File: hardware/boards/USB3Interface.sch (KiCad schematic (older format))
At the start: 5 parts

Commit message: Updated part mfr and added the proper part numbers
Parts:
- removed J?: USB3_B, symbol Connector:USB3_B
- added J?: USB3_Micro_B_Amphenol, lethalbit:USB3_Micro_B_Amphenol, symbol lethalbit:USB3_Micro_B_Amphenol
- U?: value ECP5UM5G-381caBGA -> CYUSB3014; MFR (none) -> Lattice; MPN (none) -> LFE5UM5G-85F-8BG381I
- U? (x2): MFR (none) -> Cypress; MPN (none) -> CYUSB3014-BZXI
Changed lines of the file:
@@
 AR Path="/5F2CAFD2/5F2EB784" Ref="U?"  Part="3"
 F 0 "U?" H 9800 1548 50  0000 C CNN
-F 1 "ECP5UM5G-381caBGA" H 9800 1457 50  0000 C CNN
+F 1 "CYUSB3014" H 9800 1457 50  0000 C CNN
 F 2 "" H 8450 1350 50  0001 C CNN
 F 3 "" H 8450 1350 50  0001 C CNN
+F 4 "Lattice" H 9800 1200 50  0001 C CNN "MFR"
+F 5 "LFE5UM5G-85F-8BG381I" H 9800 1200 50  0001 C CNN "MPN"
 	3    9800 1200
 	1    0    0    -1
@@
 F 2 "" H 6400 4050 50  0001 C CNN
 F 3 "" H 6400 4050 50  0001 C CNN
+F 4 "Cypress" H 6400 3350 50  0001 C CNN "MFR"
+F 5 " CYUSB3014-BZXI" H 6400 3350 50  0001 C CNN "MPN"
 	2    6400 3350
 	1    0    0    -1
@@
 F 2 "" H 3050 2400 50  0001 C CNN
 F 3 "" H 3050 2400 50  0001 C CNN
+F 4 "Cypress" H 3050 1700 50  0001 C CNN "MFR"
+F 5 " CYUSB3014-BZXI" H 3050 1700 50  0001 C CNN "MPN"
 	3    3050 1700
 	1    0    0    -1
@@
 $EndComp
 $Comp
-L Connector:USB3_B J?
-U 1 1 5F338E59
-P 1200 1450
-F 0 "J?" H 1257 2167 50  0000 C CNN
-F 1 "USB3_B" H 1257 2076 50  0000 C CNN
-F 2 "" H 1350 1550 50  0001 C CNN
-F 3 "~" H 1350 1550 50  0001 C CNN
-	1    1200 1450
+L lethalbit:USB3_Micro_B_Amphenol J?
+U 1 1 5F8A43B9
+P 3050 2600
+F 0 "J?" H 3050 3125 50  0000 C CNN
+F 1 "USB3_Micro_B_Amphenol" H 3050 3034 50  0000 C CNN
+F 2 "lethalbit:USB3_Micro_B_Amphenol" H 3050 3050 50  0001 C CNN
+F 3 "https://www.amphenol-icc.com/media/wysiwyg/files/drawing/gsb343k33hr.pdf" H 3050 3050 50  0001 C CNN
+F 4 "Amphenol" H 3050 3050 50  0001 C CNN "MFR"
+F 5 "GSB343K33HR" H 3050 3050 50  0001 C CNN "MPN"
+	1    3050 2600
 	1    0    0    -1
 $EndComp

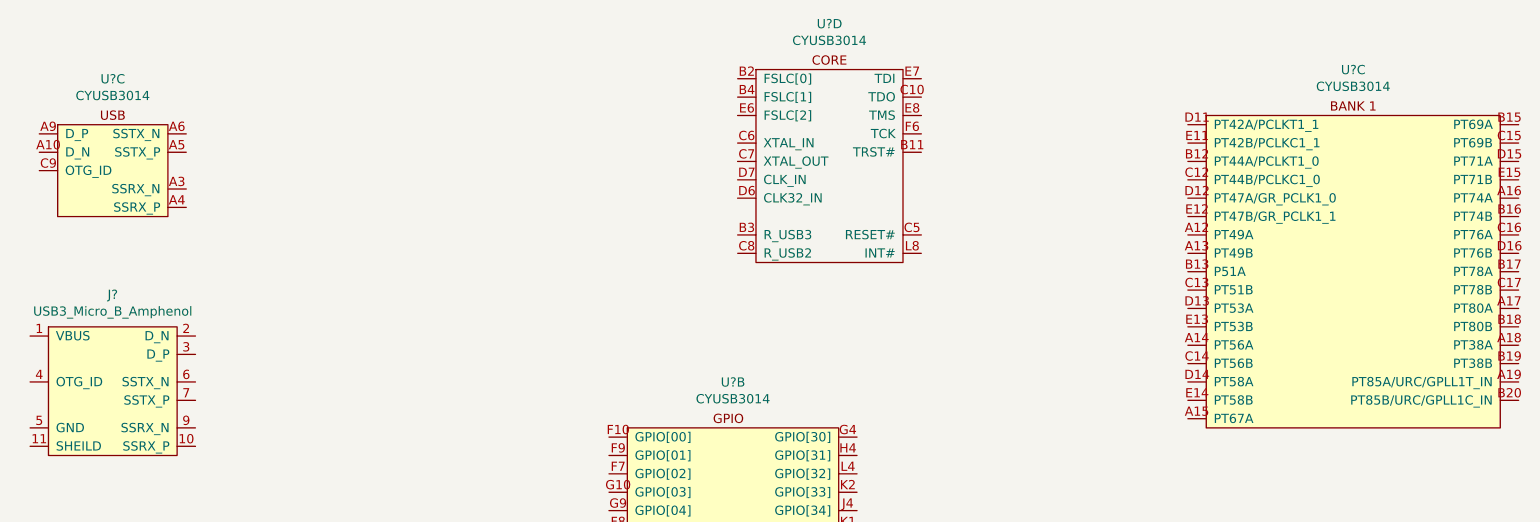
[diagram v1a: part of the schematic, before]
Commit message: Did some annotation and fixed the FPGA bank that was accidentally labled as the cypress part
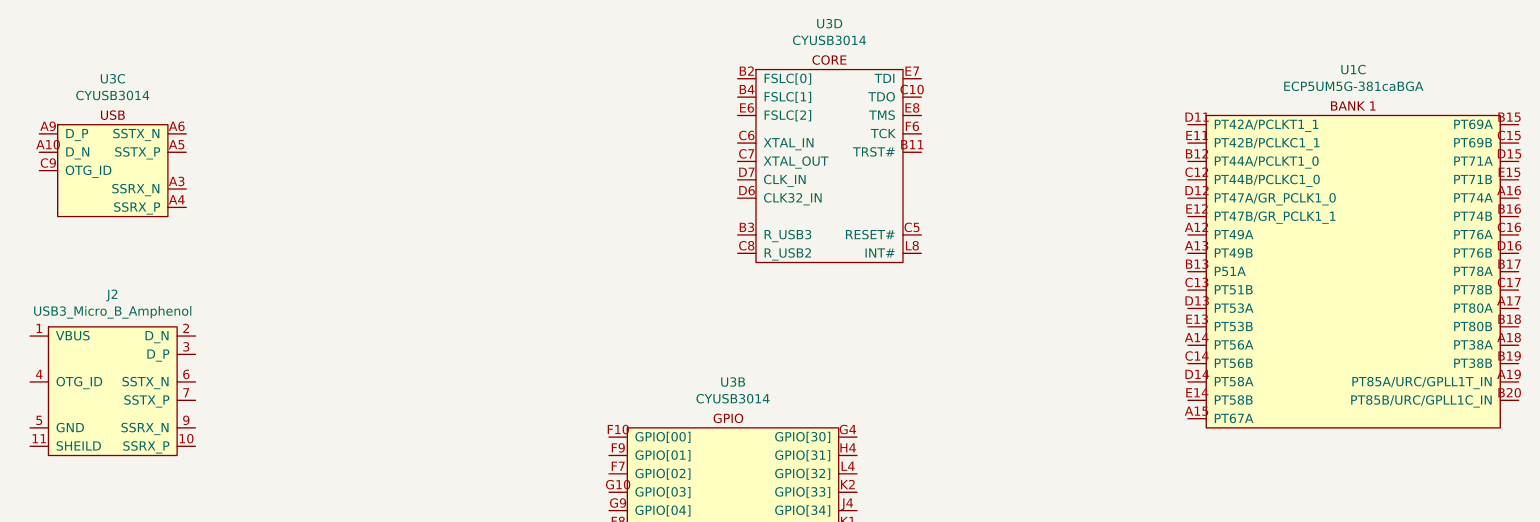
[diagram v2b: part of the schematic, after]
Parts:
- U1: renamed from U?; value CYUSB3014 -> ECP5UM5G-381caBGA; footprint (none) -> lethalbit:318caBGA
- U3: renamed from U?; footprint (none) -> lethalbit:BGA-121_11x11_10.0x10.0mm
- U3: renamed from U?; footprint (none) -> lethalbit:BGA-121_11x11_10.0x10.0mm; MFR (none) -> Cypress; MPN (none) -> https://www.cypress.com/file/140296/download
- gave numbers to parts that had none: 1
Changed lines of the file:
@@
 P 9800 1200
 AR Path="/5F2EB784" Ref="U?"  Part="3"
-AR Path="/5F2CAFD2/5F2EB784" Ref="U?"  Part="3"
-F 0 "U?" H 9800 1548 50  0000 C CNN
-F 1 "CYUSB3014" H 9800 1457 50  0000 C CNN
-F 2 "" H 8450 1350 50  0001 C CNN
+AR Path="/5F2CAFD2/5F2EB784" Ref="U1"  Part="3"
+F 0 "U1" H 9800 1548 50  0000 C CNN
+F 1 "ECP5UM5G-381caBGA" H 9800 1457 50  0000 C CNN
+F 2 "lethalbit:318caBGA" H 8450 1350 50  0001 C CNN
 F 3 "" H 8450 1350 50  0001 C CNN
 F 4 "Lattice" H 9800 1200 50  0001 C CNN "MFR"
@@
 $EndComp
 $Comp
-L lethalbit:CYUSB3014 U?
+L lethalbit:CYUSB3014 U3
 U 2 1 5F3318A9
 P 6400 3350
-F 0 "U?" H 6425 4148 50  0000 C CNN
+F 0 "U3" H 6425 4148 50  0000 C CNN
 F 1 "CYUSB3014" H 6425 4057 50  0000 C CNN
-F 2 "" H 6400 4050 50  0001 C CNN
-F 3 "" H 6400 4050 50  0001 C CNN
+F 2 "lethalbit:BGA-121_11x11_10.0x10.0mm" H 6400 4050 50  0001 C CNN
+F 3 "https://www.cypress.com/file/140296/download" H 6400 4050 50  0001 C CNN
 F 4 "Cypress" H 6400 3350 50  0001 C CNN "MFR"
 F 5 " CYUSB3014-BZXI" H 6400 3350 50  0001 C CNN "MPN"
@@
 $EndComp
 $Comp
-L lethalbit:CYUSB3014 U?
+L lethalbit:CYUSB3014 U3
 U 3 1 5F3336EC
 P 3050 1700
-F 0 "U?" H 3050 2498 50  0000 C CNN
+F 0 "U3" H 3050 2498 50  0000 C CNN
 F 1 "CYUSB3014" H 3050 2407 50  0000 C CNN
-F 2 "" H 3050 2400 50  0001 C CNN
-F 3 "" H 3050 2400 50  0001 C CNN
+F 2 "lethalbit:BGA-121_11x11_10.0x10.0mm" H 3050 2400 50  0001 C CNN
+F 3 "https://www.cypress.com/file/140296/download" H 3050 2400 50  0001 C CNN
 F 4 "Cypress" H 3050 1700 50  0001 C CNN "MFR"
 F 5 " CYUSB3014-BZXI" H 3050 1700 50  0001 C CNN "MPN"
@@
 $EndComp
 $Comp
-L lethalbit:CYUSB3014 U?
+L lethalbit:CYUSB3014 U3
 U 4 1 5F335021
 P 6950 1400
-F 0 "U?" H 6950 2198 50  0000 C CNN
+F 0 "U3" H 6950 2198 50  0000 C CNN
 F 1 "CYUSB3014" H 6950 2107 50  0000 C CNN
-F 2 "" H 6950 2100 50  0001 C CNN
-F 3 "" H 6950 2100 50  0001 C CNN
+F 2 "lethalbit:BGA-121_11x11_10.0x10.0mm" H 6950 2100 50  0001 C CNN
+F 3 "https://www.cypress.com/file/140296/download" H 6950 2100 50  0001 C CNN
+F 4 "Cypress" H 6950 1400 50  0001 C CNN "MFR"
+F 5 "https://www.cypress.com/file/140296/download" H 6950 1400 50  0001 C CNN "MPN"
 	4    6950 1400
 	1    0    0    -1
 $EndComp
 $Comp
-L lethalbit:USB3_Micro_B_Amphenol J?
+L lethalbit:USB3_Micro_B_Amphenol J2
 U 1 1 5F8A43B9
 P 3050 2600
-F 0 "J?" H 3050 3125 50  0000 C CNN
+F 0 "J2" H 3050 3125 50  0000 C CNN
 F 1 "USB3_Micro_B_Amphenol" H 3050 3034 50  0000 C CNN
 F 2 "lethalbit:USB3_Micro_B_Amphenol" H 3050 3050 50  0001 C CNN

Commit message: Some more mist schematic edits
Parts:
- J2: DIGIKEY_PN (none) -> GSB343K33HRCT-ND
- U1: DIGIKEY_PN (none) -> 220-2112-ND
- U3: DIGIKEY_PN (none) -> 428-3130-ND
- U3: DIGIKEY_PN (none) -> 428-3130-ND; MPN https://www.cypress.com/file/140296/download -> CYUSB3014-BZXI
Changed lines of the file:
@@
 F 4 "Lattice" H 9800 1200 50  0001 C CNN "MFR"
 F 5 "LFE5UM5G-85F-8BG381I" H 9800 1200 50  0001 C CNN "MPN"
+F 6 "220-2112-ND" H 9800 1200 50  0001 C CNN "DIGIKEY_PN"
 	3    9800 1200
 	1    0    0    -1
@@
 F 4 "Cypress" H 6400 3350 50  0001 C CNN "MFR"
 F 5 " CYUSB3014-BZXI" H 6400 3350 50  0001 C CNN "MPN"
+F 6 "428-3130-ND" H 6400 3350 50  0001 C CNN "DIGIKEY_PN"
 	2    6400 3350
 	1    0    0    -1
@@
 F 4 "Cypress" H 3050 1700 50  0001 C CNN "MFR"
 F 5 " CYUSB3014-BZXI" H 3050 1700 50  0001 C CNN "MPN"
+F 6 "428-3130-ND" H 3050 1700 50  0001 C CNN "DIGIKEY_PN"
 	3    3050 1700
 	1    0    0    -1
@@
 F 3 "https://www.cypress.com/file/140296/download" H 6950 2100 50  0001 C CNN
 F 4 "Cypress" H 6950 1400 50  0001 C CNN "MFR"
-F 5 "https://www.cypress.com/file/140296/download" H 6950 1400 50  0001 C CNN "MPN"
+F 5 " CYUSB3014-BZXI" H 6950 1400 50  0001 C CNN "MPN"
+F 6 "428-3130-ND" H 6950 1400 50  0001 C CNN "DIGIKEY_PN"
 	4    6950 1400
 	1    0    0    -1
@@
 F 4 "Amphenol" H 3050 3050 50  0001 C CNN "MFR"
 F 5 "GSB343K33HR" H 3050 3050 50  0001 C CNN "MPN"
+F 6 "GSB343K33HRCT-ND" H 3050 2600 50  0001 C CNN "DIGIKEY_PN"
 	1    3050 2600
 	1    0    0    -1

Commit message: Lots of small updates, getting values specified for parts, switched the BJT to NFETs
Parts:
- added C39: 0.1uF, Capacitor_SMD:C_0603_1608Metric, symbol Device:C_Small
- added R35: 1M, Resistor_SMD:R_0603_1608Metric, symbol Device:R_Small
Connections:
- net at U3.A10 (D_N): now also J2.2 (D_N)
- net at U3.A3 (SSRX_N): now also J2.9 (SSRX_N)
- net at U3.A4 (SSRX_P): now also J2.10 (SSRX_P)
- net at U3.A5 (SSTX_P): now also J2.7 (SSTX_P)
- net at U3.A6 (SSTX_N): now also J2.6 (SSTX_N)
- net at U3.A9 (D_P): now also J2.3 (D_P)
- net at J2.11 (SHEILD): now also C39.2, R35.1
- net GND: now reaches J2.5 (GND), J2.8 (GND)
- net GND: now also C39.1, R35.2
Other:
- moved on the sheet: J2, U1C, U3B, U3D
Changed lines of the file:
@@
 $Descr A4 11693 8268
 encoding utf-8
-Sheet 10 11
+Sheet 7 10
 Title ""
 Date ""
@@
 L lethalbit:ECP5UM5G-381caBGA U?
 U 3 1 5F2EB784
-P 9800 1200
+P 7950 3750
 AR Path="/5F2EB784" Ref="U?"  Part="3"
 AR Path="/5F2CAFD2/5F2EB784" Ref="U1"  Part="3"
-F 0 "U1" H 9800 1548 50  0000 C CNN
-F 1 "ECP5UM5G-381caBGA" H 9800 1457 50  0000 C CNN
-F 2 "lethalbit:318caBGA" H 8450 1350 50  0001 C CNN
-F 3 "" H 8450 1350 50  0001 C CNN
-F 4 "Lattice" H 9800 1200 50  0001 C CNN "MFR"
-F 5 "LFE5UM5G-85F-8BG381I" H 9800 1200 50  0001 C CNN "MPN"
-F 6 "220-2112-ND" H 9800 1200 50  0001 C CNN "DIGIKEY_PN"
-	3    9800 1200
+F 0 "U1" H 7950 4098 50  0000 C CNN
+F 1 "ECP5UM5G-381caBGA" H 7950 4007 50  0000 C CNN
+F 2 "lethalbit:318caBGA" H 6600 3900 50  0001 C CNN
+F 3 "" H 6600 3900 50  0001 C CNN
+F 4 "Lattice" H 7950 3750 50  0001 C CNN "MFR"
+F 5 "LFE5UM5G-85F-8BG381I" H 7950 3750 50  0001 C CNN "MPN"
+F 6 "220-2112-ND" H 7950 3750 50  0001 C CNN "DIGIKEY_PN"
+	3    7950 3750
 	1    0    0    -1
 $EndComp
@@
 L lethalbit:CYUSB3014 U3
 U 2 1 5F3318A9
-P 6400 3350
-F 0 "U3" H 6425 4148 50  0000 C CNN
-F 1 "CYUSB3014" H 6425 4057 50  0000 C CNN
-F 2 "lethalbit:BGA-121_11x11_10.0x10.0mm" H 6400 4050 50  0001 C CNN
-F 3 "https://www.cypress.com/file/140296/download" H 6400 4050 50  0001 C CNN
-F 4 "Cypress" H 6400 3350 50  0001 C CNN "MFR"
-F 5 " CYUSB3014-BZXI" H 6400 3350 50  0001 C CNN "MPN"
-F 6 "428-3130-ND" H 6400 3350 50  0001 C CNN "DIGIKEY_PN"
-	2    6400 3350
+P 4350 4050
+F 0 "U3" H 4375 4848 50  0000 C CNN
+F 1 "CYUSB3014" H 4375 4757 50  0000 C CNN
+F 2 "lethalbit:BGA-121_11x11_10.0x10.0mm" H 4350 4750 50  0001 C CNN
+F 3 "https://www.cypress.com/file/140296/download" H 4350 4750 50  0001 C CNN
+F 4 "Cypress" H 4350 4050 50  0001 C CNN "MFR"
+F 5 " CYUSB3014-BZXI" H 4350 4050 50  0001 C CNN "MPN"
+F 6 "428-3130-ND" H 4350 4050 50  0001 C CNN "DIGIKEY_PN"
+	2    4350 4050
 	1    0    0    -1
 $EndComp
@@
 L lethalbit:CYUSB3014 U3
 U 4 1 5F335021
-P 6950 1400
-F 0 "U3" H 6950 2198 50  0000 C CNN
-F 1 "CYUSB3014" H 6950 2107 50  0000 C CNN
-F 2 "lethalbit:BGA-121_11x11_10.0x10.0mm" H 6950 2100 50  0001 C CNN
-F 3 "https://www.cypress.com/file/140296/download" H 6950 2100 50  0001 C CNN
-F 4 "Cypress" H 6950 1400 50  0001 C CNN "MFR"
-F 5 " CYUSB3014-BZXI" H 6950 1400 50  0001 C CNN "MPN"
-F 6 "428-3130-ND" H 6950 1400 50  0001 C CNN "DIGIKEY_PN"
-	4    6950 1400
+P 6750 1650
+F 0 "U3" H 6750 2448 50  0000 C CNN
+F 1 "CYUSB3014" H 6750 2357 50  0000 C CNN
+F 2 "lethalbit:BGA-121_11x11_10.0x10.0mm" H 6750 2350 50  0001 C CNN
+F 3 "https://www.cypress.com/file/140296/download" H 6750 2350 50  0001 C CNN
+F 4 "Cypress" H 6750 1650 50  0001 C CNN "MFR"
+F 5 " CYUSB3014-BZXI" H 6750 1650 50  0001 C CNN "MPN"
+F 6 "428-3130-ND" H 6750 1650 50  0001 C CNN "DIGIKEY_PN"
+	4    6750 1650
 	1    0    0    -1
 $EndComp
@@
 L lethalbit:USB3_Micro_B_Amphenol J2
 U 1 1 5F8A43B9
-P 3050 2600
-F 0 "J2" H 3050 3125 50  0000 C CNN
-F 1 "USB3_Micro_B_Amphenol" H 3050 3034 50  0000 C CNN
-F 2 "lethalbit:USB3_Micro_B_Amphenol" H 3050 3050 50  0001 C CNN
-F 3 "https://www.amphenol-icc.com/media/wysiwyg/files/drawing/gsb343k33hr.pdf" H 3050 3050 50  0001 C CNN
-F 4 "Amphenol" H 3050 3050 50  0001 C CNN "MFR"
-F 5 "GSB343K33HR" H 3050 3050 50  0001 C CNN "MPN"
-F 6 "GSB343K33HRCT-ND" H 3050 2600 50  0001 C CNN "DIGIKEY_PN"
-	1    3050 2600
+P 1900 1800
+F 0 "J2" H 1900 2325 50  0000 C CNN
+F 1 "USB3_Micro_B_Amphenol" H 1900 2234 50  0000 C CNN
+F 2 "lethalbit:USB3_Micro_B_Amphenol" H 1900 2250 50  0001 C CNN
+F 3 "https://www.amphenol-icc.com/media/wysiwyg/files/drawing/gsb343k33hr.pdf" H 1900 2250 50  0001 C CNN
+F 4 "Amphenol" H 1900 2250 50  0001 C CNN "MFR"
+F 5 "GSB343K33HR" H 1900 2250 50  0001 C CNN "MPN"
+F 6 "GSB343K33HRCT-ND" H 1900 1800 50  0001 C CNN "DIGIKEY_PN"
+	1    1900 1800
 	1    0    0    -1
 $EndComp
+Wire Wire Line
+	3450 1200 3750 1200
+Wire Wire Line
+	3750 1200 3750 1750
+Wire Wire Line
+	3750 1750 2350 1750
+Wire Wire Line
+	2350 1850 3700 1850
+Wire Wire Line
+	3700 1850 3700 1300
+Wire Wire Line
+	3700 1300 3450 1300
+Wire Wire Line
+	3450 1500 3600 1500
+Wire Wire Line
+	3600 1500 3600 2000
+Wire Wire Line
+	3600 2000 2350 2000
+Wire Wire Line
+	2350 1500 2450 1500
+Wire Wire Line
+	2450 1500 2450 1300
+Wire Wire Line
+	2450 1300 2650 1300
+Wire Wire Line
+	2350 1600 2500 1600
+Wire Wire Line
+	2500 1600 2500 1200
+Wire Wire Line
+	2500 1200 2650 1200
+Wire Wire Line
+	3450 1600 3550 1600
+Wire Wire Line
+	3550 1600 3550 2100
+Wire Wire Line
+	2350 2100 3550 2100
+$Comp
+L power:GND #PWR0118
+U 1 1 5EDDAAAC
+P 1000 2700
+F 0 "#PWR0118" H 1000 2450 50  0001 C CNN
+F 1 "GND" H 1005 2527 50  0000 C CNN
+F 2 "" H 1000 2700 50  0001 C CNN
+F 3 "" H 1000 2700 50  0001 C CNN
+	1    1000 2700
+	1    0    0    -1
+$EndComp
+Wire Wire Line
+	1450 2000 1000 2000
+Wire Wire Line
+	1000 2000 1000 2350
+$Comp
+L Device:R_Small R?
+U 1 1 5EDFF9C0
+P 1200 2350
+AR Path="/5EDF9F51/5EDFF9C0" Ref="R?"  Part="1"
+AR Path="/5F2CAFD2/5EDFF9C0" Ref="R35"  Part="1"
+F 0 "R35" V 1004 2350 50  0000 C CNN
+F 1 "1M" V 1095 2350 50  0000 C CNN
+F 2 "Resistor_SMD:R_0603_1608Metric" H 1200 2350 50  0001 C CNN
+F 3 "~" H 1200 2350 50  0001 C CNN
+F 4 "Vishay Dale" V 1200 2350 50  0001 C CNN "MFR"
+F 5 "CRCW06031M00FKEA" V 1200 2350 50  0001 C CNN "MPN"
+	1    1200 2350
+	0    1    1    0
+$EndComp
+$Comp
+L Device:C_Small C?
+U 1 1 5EDFF9C8
+P 1200 2550
+AR Path="/5EDF9F51/5EDFF9C8" Ref="C?"  Part="1"
+AR Path="/5F2CAFD2/5EDFF9C8" Ref="C39"  Part="1"
+F 0 "C39" H 1108 2504 50  0000 R CNN
+F 1 "0.1uF" H 1108 2595 50  0000 R CNN
+F 2 "Capacitor_SMD:C_0603_1608Metric" H 1200 2550 50  0001 C CNN
+F 3 "~" H 1200 2550 50  0001 C CNN
+F 4 "KEMET" V 1200 2550 50  0001 C CNN "MFR"
+F 5 "C0603C104M5RACTU" V 1200 2550 50  0001 C CNN "MPN"
+	1    1200 2550
+	0    -1   -1   0
+$EndComp
+Wire Wire Line
+	1100 2550 1000 2550
+Connection ~ 1000 2550
+Wire Wire Line
+	1000 2550 1000 2700
+Wire Wire Line
+	1100 2350 1000 2350
+Connection ~ 1000 2350
+Wire Wire Line
+	1000 2350 1000 2550
+Wire Wire Line
+	1450 2100 1400 2100
+Wire Wire Line
+	1400 2100 1400 2350
+Wire Wire Line
+	1400 2550 1300 2550
+Wire Wire Line
+	1300 2350 1400 2350
+Connection ~ 1400 2350
+Wire Wire Line
+	1400 2350 1400 2550
 $EndSCHEMATC

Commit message: Some strugglebusting on getting the ERC errors cleaned up a bit
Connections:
- no-connect marks 0 -> 112
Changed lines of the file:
@@
 $Descr A4 11693 8268
 encoding utf-8
-Sheet 7 10
+Sheet 6 10
 Title "lethallink"
 Date "2020-06-13"
@@
 Wire Wire Line
 	1400 2350 1400 2550
+NoConn ~ 1450 1750
+NoConn ~ 1450 1500
+NoConn ~ 2650 1400
+NoConn ~ 6250 1150
+NoConn ~ 6250 1250
+NoConn ~ 6250 1350
+NoConn ~ 6250 1500
+NoConn ~ 6250 1600
+NoConn ~ 6250 1700
+NoConn ~ 6250 1800
+NoConn ~ 6250 2000
+NoConn ~ 6250 2100
+NoConn ~ 7250 2100
+NoConn ~ 7250 2000
+NoConn ~ 7250 1550
+NoConn ~ 7250 1450
+NoConn ~ 7250 1350
+NoConn ~ 7250 1250
+NoConn ~ 7250 1150
+NoConn ~ 3700 3550
+NoConn ~ 3700 3650
+NoConn ~ 3700 3750
+NoConn ~ 3700 3850
+NoConn ~ 3700 3950
+NoConn ~ 3700 4050
+NoConn ~ 3700 4150
+NoConn ~ 3700 4250
+NoConn ~ 3700 4350
+NoConn ~ 3700 4450
+NoConn ~ 3700 4550
+NoConn ~ 3700 4650
+NoConn ~ 3700 4750
+NoConn ~ 3700 4850
+NoConn ~ 3700 4950
+NoConn ~ 3700 5050
+NoConn ~ 3700 5150
+NoConn ~ 3700 5250
+NoConn ~ 3700 5350
+NoConn ~ 3700 5450
+NoConn ~ 3700 5550
+NoConn ~ 3700 5650
+NoConn ~ 3700 5750
+NoConn ~ 3700 5850
+NoConn ~ 3700 5950
+NoConn ~ 3700 6050
+NoConn ~ 3700 6150
+NoConn ~ 3700 6250
+NoConn ~ 3700 6350
+NoConn ~ 3700 6450
+NoConn ~ 5050 6450
+NoConn ~ 5050 6350
+NoConn ~ 5050 6250
+NoConn ~ 5050 6150
+NoConn ~ 5050 6050
+NoConn ~ 5050 5950
+NoConn ~ 5050 5850
+NoConn ~ 5050 5750
+NoConn ~ 5050 5650
+NoConn ~ 5050 5550
+NoConn ~ 5050 5450
+NoConn ~ 5050 5350
+NoConn ~ 5050 5250
+NoConn ~ 5050 5150
+NoConn ~ 5050 5050
+NoConn ~ 5050 4950
+NoConn ~ 5050 4850
+NoConn ~ 5050 4750
+NoConn ~ 5050 4650
+NoConn ~ 5050 4550
+NoConn ~ 5050 4450
+NoConn ~ 5050 4350
+NoConn ~ 5050 4250
+NoConn ~ 5050 4150
+NoConn ~ 5050 4050
+NoConn ~ 5050 3950
+NoConn ~ 5050 3850
+NoConn ~ 5050 3750
+NoConn ~ 5050 3650
+NoConn ~ 5050 3550
+NoConn ~ 7050 3700
+NoConn ~ 7050 3800
+NoConn ~ 7050 3900
+NoConn ~ 7050 4000
+NoConn ~ 7050 4100
+NoConn ~ 7050 4200
+NoConn ~ 7050 4300
+NoConn ~ 7050 4400
+NoConn ~ 7050 4500
+NoConn ~ 7050 4600
+NoConn ~ 7050 4750
+NoConn ~ 7050 4800
+NoConn ~ 7050 4900
+NoConn ~ 7050 5000
+NoConn ~ 7050 5100
+NoConn ~ 7050 5200
+NoConn ~ 7050 5300
+NoConn ~ 8850 5200
+NoConn ~ 8850 5100
+NoConn ~ 8850 5000
+NoConn ~ 8850 4900
+NoConn ~ 8850 4800
+NoConn ~ 8850 4700
+NoConn ~ 8850 4600
+NoConn ~ 8850 4500
+NoConn ~ 8850 4400
+NoConn ~ 8850 4300
+NoConn ~ 8850 4200
+NoConn ~ 8850 4100
+NoConn ~ 8850 4000
+NoConn ~ 8850 3900
+NoConn ~ 8850 3800
+NoConn ~ 8850 3700
 $EndSCHEMATC
